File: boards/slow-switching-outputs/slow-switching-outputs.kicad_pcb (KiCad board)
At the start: 2 copper layers, 80 x 60 mm, 24 parts, among them J1 POWER, J2 Conn_01x02_Male, J3 Conn_01x02_Male, J4 Conn_01x02_Male, J5 Conn_01x03_Male, J6 Conn_01x03_Male, Q1 TIP122, Q2 PN2222A, U1 PC817, U2 PC817

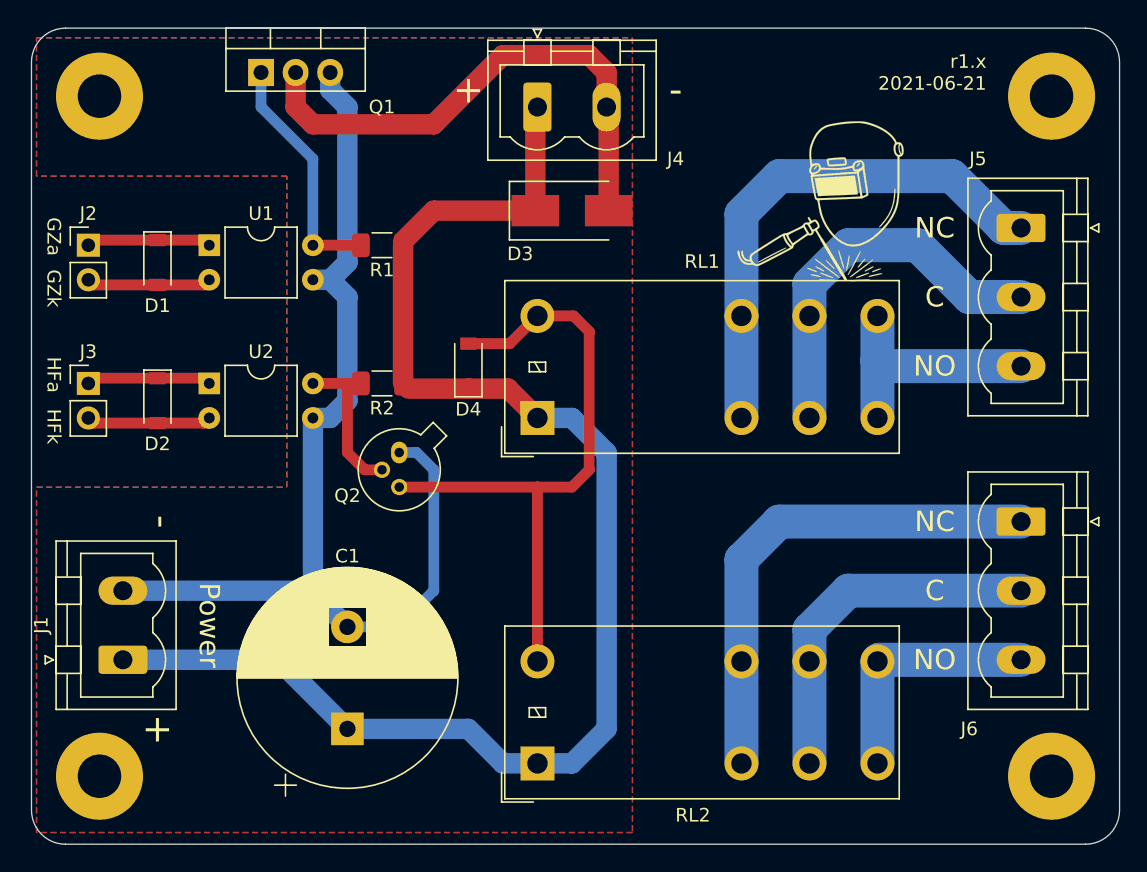
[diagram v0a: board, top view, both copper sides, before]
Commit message: slow-switching-outputs: updated to kicad 7
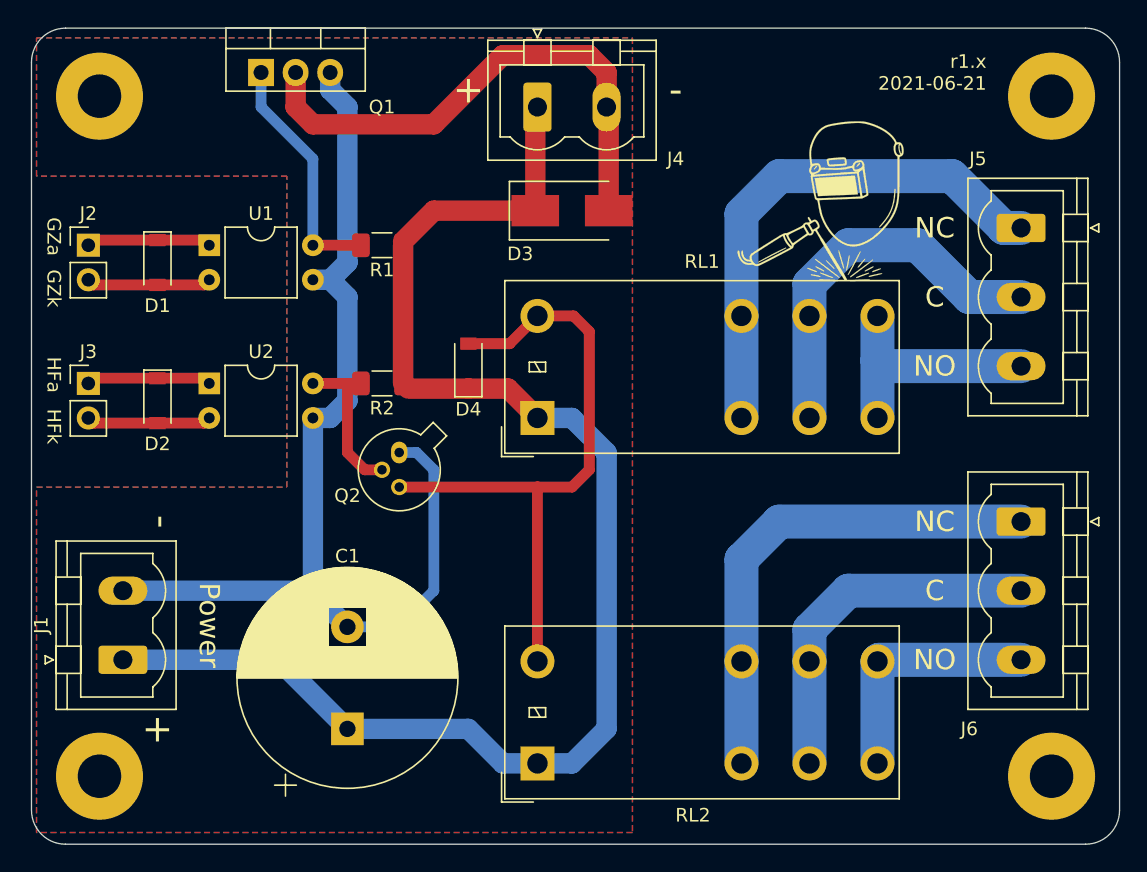
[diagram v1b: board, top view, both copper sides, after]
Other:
- net class Default removed
